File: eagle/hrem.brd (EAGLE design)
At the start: 34.1 x 60 mm, 7 parts, among them U1 TINY85-20-DIP

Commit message: PCB improvements
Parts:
- removed C1: 22uF, SparkFun-Capacitors:CAP-PTH-SMALL-KIT
- removed G1: CR2032H, battery:CR2032H
- added BAT1: (no value), SparkFun-Electromechanical:BATTERY-AAA
- added C2: 10uF, SparkFun-Capacitors:EIA3216
- added C3: 100uF, SparkFun-Capacitors:EIA3216
- added C4: 22uF, SparkFun-Capacitors:EIA3216
- added L1: 47uH, SparkFun-Passives:CR54
- added R2: 300K, SparkFun-Resistors:1206
- added R3: 100K, SparkFun-Resistors:1206
- added R4: 100, SparkFun-Resistors:1206
- added U$1: LM2621SMD, SparkFun-PowerIC:MSOP-8
- LED1: device led:LED3MM -> led:SML1206
- R1: device SparkFun-Resistors:AXIAL-0.4 -> SparkFun-Resistors:1206
- U1: value TINY85-20-DIP -> Tiny85-20-SMT; device SparkFun-DigitalIC:DIP08 -> SparkFun-DigitalIC:SO08-EIAJ
- moved U1 12.5 mm to (14.0, 36.0), flipped to the bottom
- moved SG2 10.8 mm to (23.0, 16.0)
- moved R1 7.07 mm to (22.0, 34.0), flipped to the bottom, turned to 180 degrees
- flipped LED1 to the bottom, turned to 270 degrees
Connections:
- new net N$10: C2.C, R4.2, U$1.8
- new net N$12: R2.2, R3.1, U$1.4
- new net N$15: BAT1.PWR@1, C4.A, L1.P$1, R4.1
- new net N$9: C2.A, L1.P$2, U$1.3
- net GND: now also BAT1.GND@1, C3.C, C4.C, LED1.C, R3.2, U$1.1, U$1.5; no longer C1.2, G1.-, LED1.K
- net N$1: now also R1.2; no longer R1.P$2
- net N$3: now also U1.3; no longer U1.2
- net N$5: now also U1.2; no longer U1.3
- net N$8: now also R1.1; no longer R1.P$1
- net VCC: now also C3.A, R2.1, U$1.2, U$1.6, U$1.7; no longer C1.1, G1.+
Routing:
- net N$9: track 0.00 -> 20.7 mm
- net N$15: track 0.00 -> 18.6 mm
- net VCC: track 21.8 -> 35.3 mm
- net N$3: track 8.50 -> 21.4 mm
- net N$8: track 4.46 -> 11.3 mm
- net N$10: track 0.00 -> 6.29 mm
- net N$12: track 0.00 -> 5.62 mm
- net N$5: track 21.8 -> 18.2 mm
- net N$1: track 6.48 -> 3.91 mm
- net V+: track 21.0 -> 19.3 mm

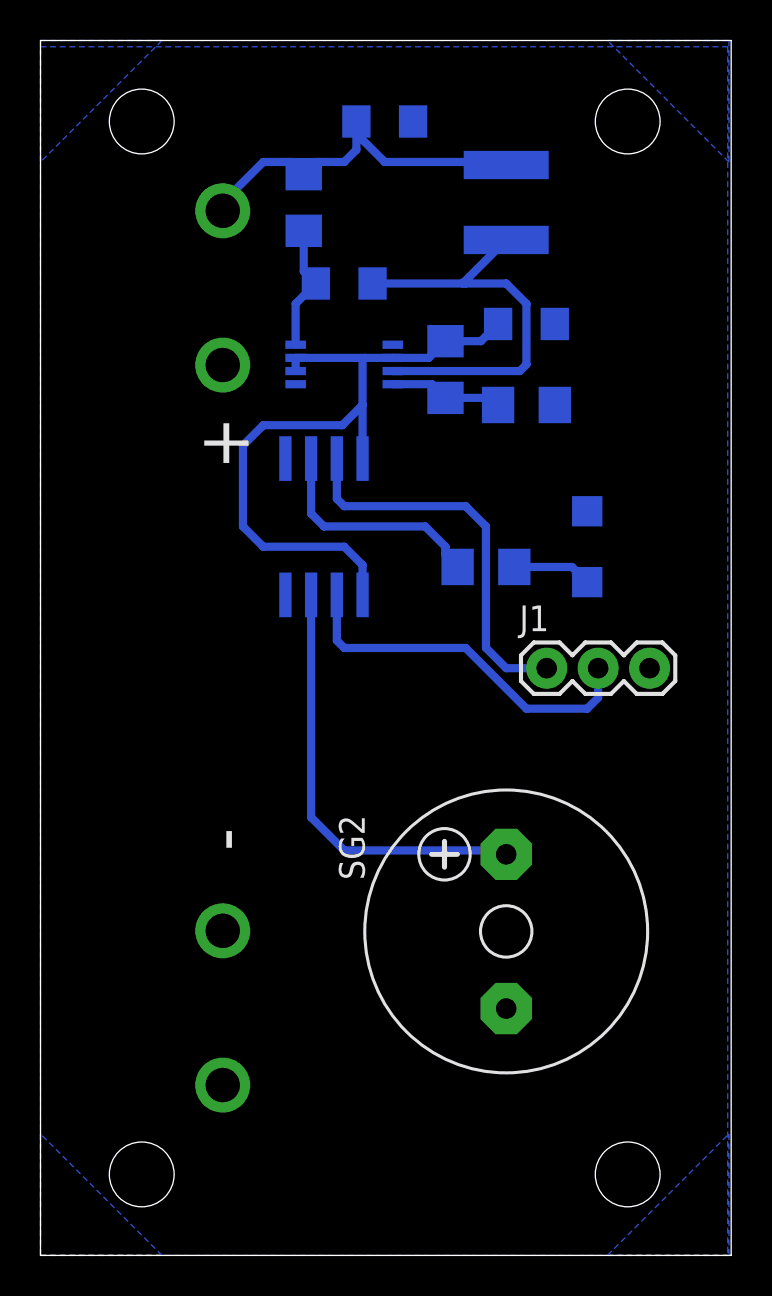
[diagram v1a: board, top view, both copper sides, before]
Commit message: SMD version
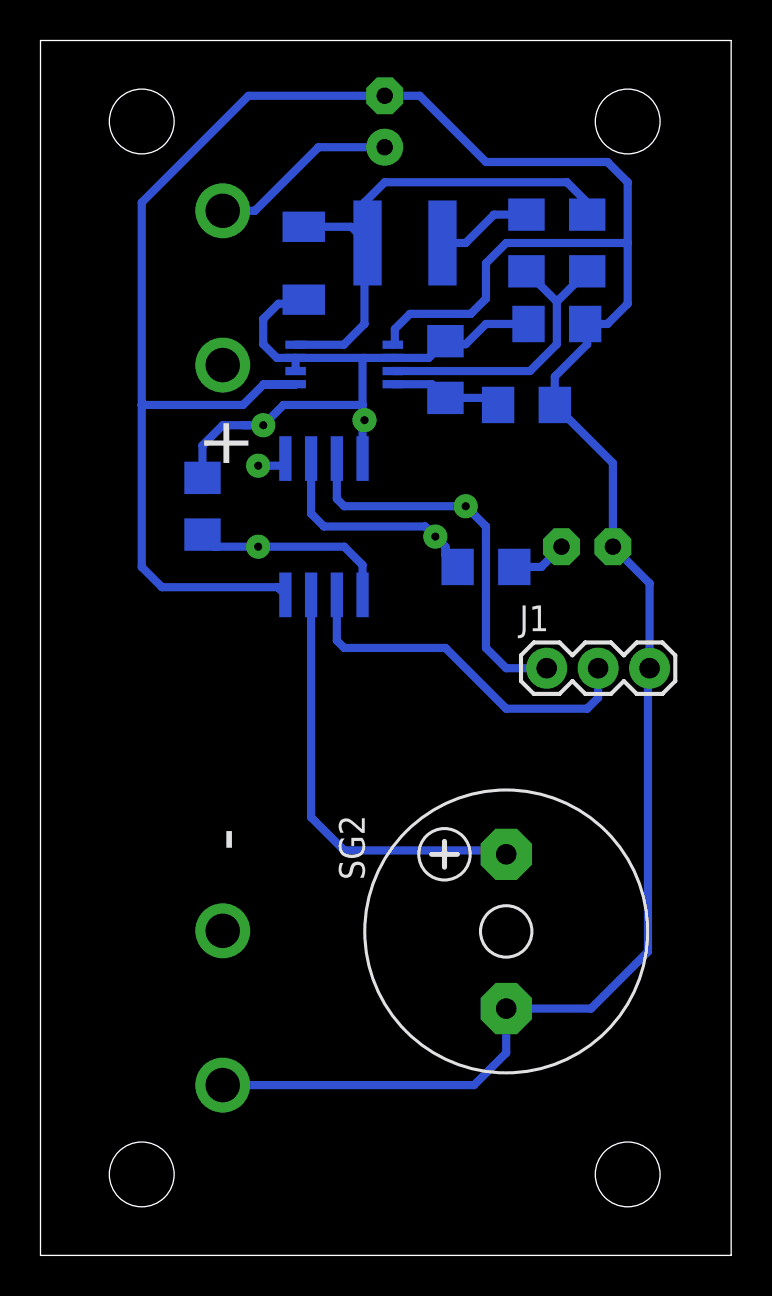
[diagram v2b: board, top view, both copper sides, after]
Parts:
- removed C2: 10uF, SparkFun-Capacitors:EIA3216
- added C1: 4.7pF, rcl:C1206
- added D1: CGRM4001-G, diode:SOD-123_MINI-SMA
- added R5: 100K, SparkFun-Resistors:1206
- C3: device SparkFun-Capacitors:EIA3216 -> rcl:C1206
- C4: device SparkFun-Capacitors:EIA3216 -> rcl:E2,5-5
- L1: value 47uH -> 4.7uH
- LED1: device led:SML1206 -> led:LED3MM
- R1: value 100 -> 200
- R4: value 100 -> 150K
- moved R4 11.2 mm to (24.0, 50.0), turned to 90 degrees
- moved L1 5.39 mm to (18.0, 50.0), turned to 270 degrees
- moved C3 1.50 mm to (25.5, 46.0), turned to 180 degrees
- turned C4 to 90 degrees
- turned LED1 to 180 degrees
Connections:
- new net N$11: C1.2, R4.1, U$1.3
- new net N$2: R5.1, U1.1
- net GND: now also C3.2, C4.-, LED1.K; no longer C3.C, C4.C, LED1.C
- net N$10: now also L1.P$2; no longer C2.C, U$1.8
- net N$15: now also C4.+; no longer C4.A, L1.P$1, R4.1
- net N$9: now also C1.1, D1.A, L1.P$1, U$1.8; no longer C2.A, L1.P$2, U$1.3
- net VCC: now also C3.1, D1.C, R5.2; no longer C3.A, U1.1
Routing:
- net GND: track 0.00 -> 145.6 mm
- net N$11: track 0.00 -> 15.0 mm
- net N$2: track 0.00 -> 10.0 mm, vias 0 -> 1
- net N$15: track 18.6 -> 9.30 mm
- net N$9: track 20.7 -> 25.9 mm
- net N$10: track 6.29 -> 4.73 mm
- net N$6: track 0.00 -> 1.25 mm, vias 0 -> 1
- net N$1: track 3.91 -> 2.74 mm
- net VCC: track 35.3 -> 34.8 mm, vias 0 -> 1
- net V+: vias 0 -> 1
- net N$8: vias 0 -> 1
- removed copper zone on layer 16, net GND
- removed copper zone on layer 16, net N$2
- removed copper zone on layer 16, net N$4
- removed copper zone on layer 16, net N$6
- removed copper zone on layer 16, net N$7
